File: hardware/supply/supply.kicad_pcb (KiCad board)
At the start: 4 copper layers, 62.4 x 125 mm, 34 parts, among them J1 Conn_01x01, J2 Screw, J3 Conn_01x01, J5 Conn_01x01, J6 Screw, J7 Conn_01x01, Q3 IRF4905PBF, Q4 BC857C, Q5 IRF4905PBF, Q6 IRF4905PBF

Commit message: replace mosfets with bjts in inrush current limiter
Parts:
- removed Q3, Q5, Q6: IRF4905PBF, Package_TO_SOT_THT:TO-220-3_Vertical
- removed R3: 80m, supply:WSHM28181L000FEA
- added Q1: TIP147, supply:TO545P515X1560X2445-3P, F.Cu at (184.5, 103.8)
- added Q2: TIP147, supply:TO545P515X1560X2445-3P, F.Cu at (184.5, 87.5)
- added R1: 70m, Resistor_SMD:R_2512_6332Metric, F.Cu at (183.9, 66.7)
- added R2: 5k, Resistor_SMD:R_0805_2012Metric, F.Cu at (184.5, 55.9)
- R4: value 30k -> 4.7k; footprint Resistor_SMD:R_1206_3216Metric -> Resistor_SMD:R_0805_2012Metric
- moved R4 3.55 mm to (186.4, 55.9)
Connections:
- Q4 pad 3: Net-(Q3-G) -> Net-(Q1-B)
- R4 pad 1: Net-(Q3-G) -> GND
- R4 pad 2: GND -> Net-(Q1-B)
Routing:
- net Net-(Q3-G): track 60.6 -> 0.00 mm, vias 1 -> 0
- net Net-(Q1-B): track 0.00 -> 59.4 mm, vias 0 -> 1
- net Net-(Q1-E): track 12.0 -> 20.9 mm
- net Net-(Q4-E): track 6.03 -> 4.72 mm
- removed copper zone on F.Cu, net Net-(Q3-S)

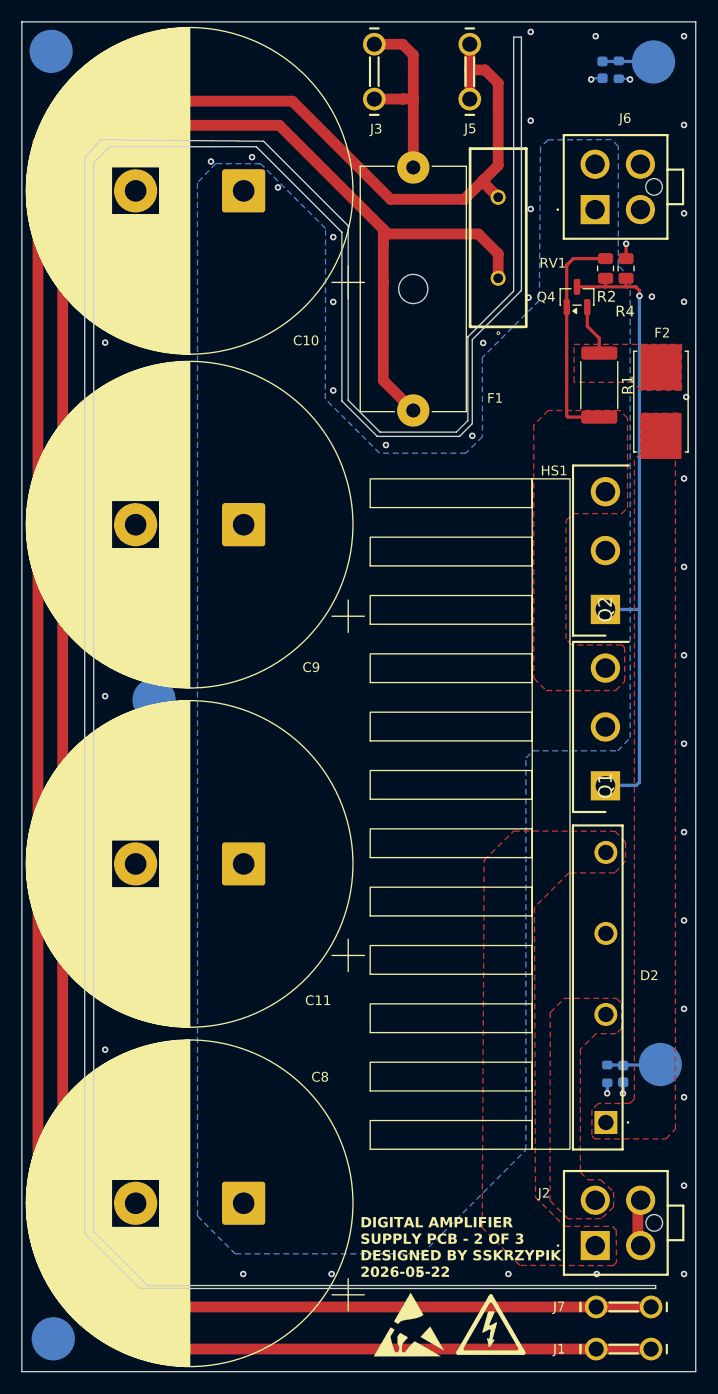
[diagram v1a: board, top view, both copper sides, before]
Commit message: swap power connectors and flip front panel PCB orientation
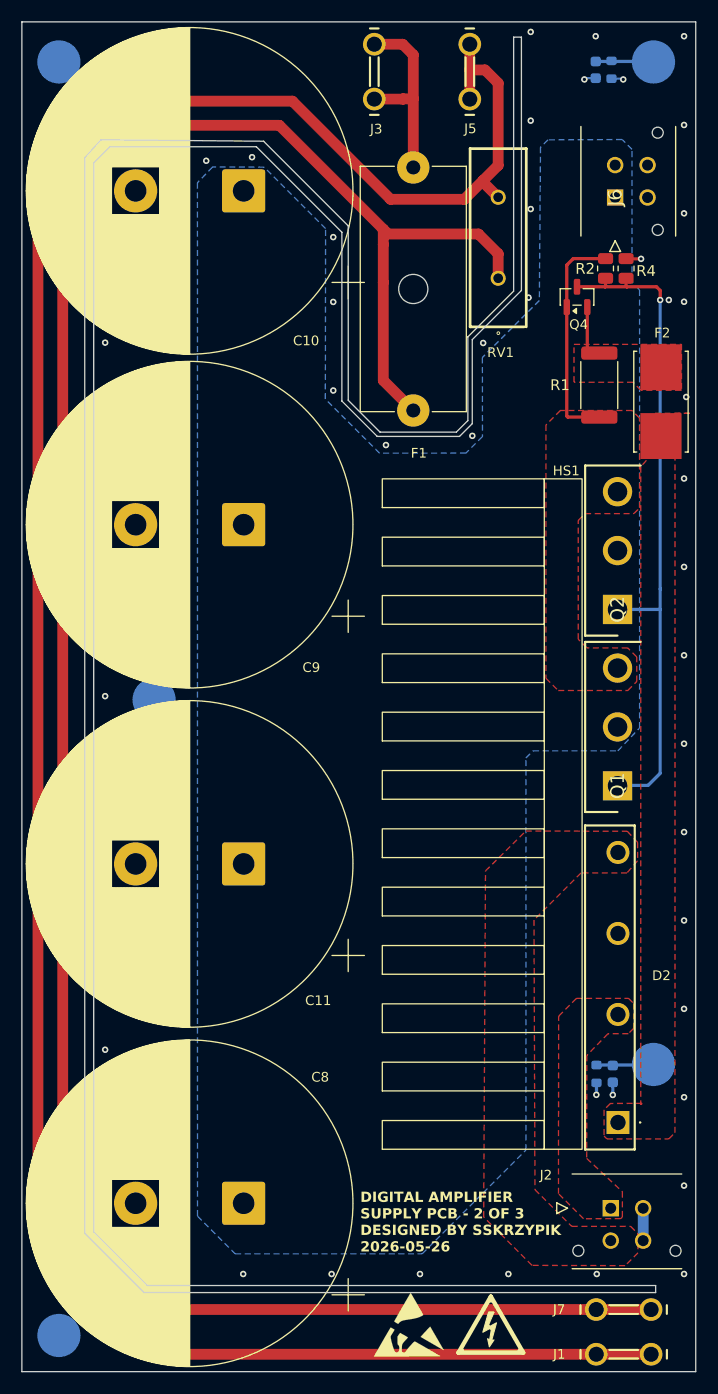
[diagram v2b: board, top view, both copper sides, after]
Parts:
- J2, J6: footprint supply:2125201004 -> supply:43045-04YY_121314
- moved J2 3.74 mm to (185.0, 142.9), turned to 180 degrees
- moved J6 2.17 mm to (185.4, 49.3)
- moved H3 1.22 mm to (133.9, 36.8)
- moved D2 1.12 mm to (185.7, 135.0)
- moved HS1 1.12 mm to (190.4, 142.5)
- moved Q1 1.12 mm to (185.6, 103.8)
- moved Q2 1.12 mm to (185.6, 87.5)
- moved R9 1.00 mm to (183.7, 130.5)
- moved C2 0.97 mm to (185.2, 130.5)
- moved C5 0.83 mm to (141.9, 101.1)
- moved R8 0.83 mm to (141.9, 99.7)
- moved R7 0.68 mm to (185.1, 37.5)
- moved C1 0.63 mm to (183.6, 37.5)
- moved H1 0.63 mm to (189.0, 129.6)
- moved H2 0.61 mm to (133.9, 154.7)
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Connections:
- D2 pad 2: Net-(J2-Pin_2) -> Net-(J2-Pin_1)
- D2 pad 4: Net-(J2-Pin_1) -> Net-(J2-Pin_3)
- J2 pad 4: Net-(J2-Pin_3) -> Net-(J2-Pin_2)
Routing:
- net Net-(Q1-B): track 59.4 -> 64.6 mm
- net Net-(J2-Pin_3): track 4.42 -> 0.00 mm
- net Net-(J2-Pin_2): track 0.00 -> 3.00 mm
- net GND: track 7.85 -> 8.15 mm, vias 56 -> 55
- added copper zone on F.Cu, net Net-(J2-Pin_3)
- removed copper zone on F.Cu, net Net-(J2-Pin_2)
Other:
- outline, holes or cut-outs redrawn
- board text added: "DIGITAL AMPLIFIER SUPPLY PCB - 2 OF 3 DESIGNED BY SSKRZYPIK 2026-05-26"
- board text removed: "DIGITAL AMPLIFIER SUPPLY PCB - 2 OF 3 DESIGNED BY SSKRZYPIK 2026-05-22"

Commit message: Prepare PCB for production
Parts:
- moved R7 2.07 mm to (183.0, 37.5)
- moved C1 2.07 mm to (181.6, 37.5)
- moved H4 2.07 mm to (186.9, 36.8)
- moved J6 2.07 mm to (183.3, 49.3)
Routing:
- net GND: track 8.15 -> 8.38 mm, vias 55 -> 54
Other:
- outline, holes or cut-outs redrawn
- board text added: "DIGITAL AMPLIFIER SUPPLY PCB - 2 OF 3 DESIGNED BY SSKRZYPIK 2026-05-30"
- board text removed: "DIGITAL AMPLIFIER SUPPLY PCB - 2 OF 3 DESIGNED BY SSKRZYPIK 2026-05-26"
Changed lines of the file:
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@@
 	(footprint "supply:43045-04YY_121314"
 		(layer "F.Cu")
-		(at 185.42 49.33 -90)
+		(at 183.35 49.33 -90)
 		(descr "43045-04YY_121314")
 		(tags "Connector")
 		(property "Reference" "J6"
-			(at 0 0 270)
+			(at 6.16 4.17 0)
 			(layer "F.SilkS")
 			(effects
@@
 	(footprint "supply:WA-SMSI_97730256330"
 		(layer "B.Cu")
-		(at 188.97 36.78)
+		(at 186.9 36.78)
 		(descr "WA-SMSI SMT Steel Spacer with internal Thread M1.6 Bottom closed Thread Internal M1.6 Height = 2.5mm Inner Thread Length = 1.5mm")
 		(property "Reference" "H4"
@@
 	(footprint "Resistor_SMD:R_0603_1608Metric"
 		(layer "B.Cu")
-		(at 185.08 37.505 90)
+		(at 183.01 37.505 90)
 		(descr "Resistor SMD 0603 (1608 Metric), square (rectangular) end terminal, IPC-7351 nominal, (Body size source: IPC-SM-782 page 72, https://www.pcb-3d.com/wordpress/wp-content/uploads/ipc-sm-782a_amendment_1_and_2.pdf)")
 		(tags "resistor")
@@
 	(footprint "Capacitor_SMD:C_0603_1608Metric"
 		(layer "B.Cu")
-		(at 183.62 37.51 -90)
+		(at 181.55 37.51 -90)
 		(descr "Capacitor SMD 0603 (1608 Metric), square (rectangular) end terminal, IPC-7351 nominal, (Body size source: IPC-SM-782 page 76, https://www.pcb-3d.com/wordpress/wp-content/uploads/ipc-sm-782a_amendment_1_and_2.pdf)")
 		(tags "capacitor")
@@
 		)
 	)
-	(gr_rect
+	(gr_line
 		(start 130.49 33.07)
+		(end 130.49 158.04)
+		(stroke
+			(width 0.05)
+			(type default)
+		)
+		(layer "Edge.Cuts")
+	)
+	(gr_line
+		(start 130.49 158.04)
 		(end 192.88 158.04)
 		(stroke
@@
 			(type default)
 		)
-		(fill no)
 		(layer "Edge.Cuts")
 	)
@@
 		(layer "Edge.Cuts")
 	)
-	(gr_text "DIGITAL AMPLIFIER\nSUPPLY PCB - 2 OF 3\nDESIGNED BY SSKRZYPIK\n2026-05-26\n"
+	(gr_line
+		(start 190.68 33.07)
+		(end 130.49 33.07)
+		(stroke
+			(width 0.05)
+			(type default)
+		)
+		(layer "Edge.Cuts")
+	)
+	(gr_line
+		(start 190.68 62.19)
+		(end 190.68 33.07)
+		(stroke
+			(width 0.05)
+			(type default)
+		)
+		(layer "Edge.Cuts")
+	)
+	(gr_line
+		(start 192.88 62.19)
+		(end 190.68 62.19)
+		(stroke
+			(width 0.05)
+			(type default)
+		)
+		(layer "Edge.Cuts")
+	)
+	(gr_line
+		(start 192.88 158.04)
+		(end 192.88 62.19)
+		(stroke
+			(width 0.05)
+			(type default)
+		)
+		(layer "Edge.Cuts")
+	)
+	(gr_text "DIGITAL AMPLIFIER\nSUPPLY PCB - 2 OF 3\nDESIGNED BY SSKRZYPIK\n2026-05-30\n"
 		(at 161.82 147.03 0)
 		(layer "F.SilkS")
@@
 	)
 	(via
-		(at 191.8 58.983333)
-		(size 0.6)
-		(drill 0.3)
-		(layers "F.Cu" "B.Cu")
-		(net "GND")
-	)
-	(via
 		(at 183.616667 34.4)
 		(size 0.6)
@@
 	)
 	(via
-		(at 182.57 38.4)
+		(at 184.035 38.335)
 		(size 0.6)
 		(drill 0.3)
@@
 	)
 	(via
-		(at 186.17 38.4)
+		(at 180.615 38.285)
 		(size 0.6)
 		(drill 0.3)
@@
 	)
 	(via
-		(at 191.8 42.616667)
+		(at 189.73 42.616667)
 		(size 0.6)
 		(drill 0.3)
@@
 	)
 	(via
-		(at 190.390003 58.82)
+		(at 188.43 58.77)
 		(size 0.6)
 		(drill 0.3)
@@
 	)
 	(via
-		(at 191.8 34.4)
+		(at 189.73 34.4)
 		(size 0.6)
 		(drill 0.3)
@@
 	)
 	(via
-		(at 191.8 50.8)
+		(at 189.73 50.8)
 		(size 0.6)
 		(drill 0.3)
@@
 	)
 	(segment
-		(start 182.685 38.285)
-		(end 182.57 38.4)
-		(width 0.2)
-		(layer "B.Cu")
-		(net "GND")
-	)
-	(segment
 		(start 141.11 101.12)
 		(end 140.11 101.12)
@@
 	)
 	(segment
-		(start 186.105 38.335)
-		(end 186.17 38.4)
-		(width 0.2)
-		(layer "B.Cu")
-		(net "GND")
-	)
-	(segment
-		(start 185.13 38.335)
-		(end 186.105 38.335)
+		(start 182.735 38.335)
+		(end 182.685 38.285)
 		(width 0.2)
 		(layer "B.Cu")
@@
 	)
 	(segment
-		(start 183.62 38.285)
-		(end 182.685 38.285)
+		(start 181.55 38.285)
+		(end 180.615 38.285)
 		(width 0.2)
 		(layer "B.Cu")
@@
 	)
 	(segment
-		(start 183.67 38.335)
-		(end 183.62 38.285)
+		(start 181.6 38.335)
+		(end 181.55 38.285)
 		(width 0.2)
 		(layer "B.Cu")
@@
 	)
 	(segment
+		(start 184.035 38.335)
+		(end 182.735 38.335)
+		(width 0.2)
+		(layer "B.Cu")
+		(net "GND")
+	)
+	(segment
+		(start 184.035 38.335)
+		(end 184.1 38.4)
+		(width 0.2)
+		(layer "B.Cu")
+		(net "GND")
+	)
+	(segment
 		(start 164.63 49.5)
 		(end 171.45 49.5)
@@
 	)
 	(segment
-		(start 183.62 36.735)
-		(end 188.295 36.735)
+		(start 181.55 36.735)
+		(end 186.225 36.735)
 		(width 0.3)
 		(layer "B.Cu")
@@
 	)
 	(segment
-		(start 188.925 36.735)
-		(end 188.97 36.78)
+		(start 186.855 36.735)
+		(end 186.9 36.78)
 		(width 0.3)
 		(layer "B.Cu")
@@
 			(pts
 				(xy 146.75 143.64) (xy 150.24 147.13) (xy 167.55 147.13) (xy 177.155283 137.524717) (xy 177.155283 101.224717)
-				(xy 177.82 100.56) (xy 185.66901 100.56) (xy 187.68 98.447261) (xy 187.68 57.903181) (xy 186.98 57.149091)
-				(xy 186.98 44.87596) (xy 186.059102 43.96315) (xy 179.199971 43.993399) (xy 178.506983 44.676075)
+				(xy 177.82 100.56) (xy 185.66901 100.56) (xy 187.68 98.447261) (xy 187.68 57.903181) (xy 184.91 54.919139)
+				(xy 184.91 44.399911) (xy 184.47641 43.970129) (xy 179.199971 43.993399) (xy 178.506983 44.676075)
 				(xy 178.400602 58.867373) (xy 173.125227 64.143671) (xy 173.134558 71.465762) (xy 171.603828 72.998327)
 				(xy 163.614576 73.001664) (xy 158.586652 67.993937) (xy 158.60958 52.200995) (xy 152.914152 46.521815)
